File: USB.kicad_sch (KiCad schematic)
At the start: 38 parts, among them J1 DX07S024JJ2R1300, Q6 AGM612AP, Q7 AO3404A, U3 TPD4S480RUKR

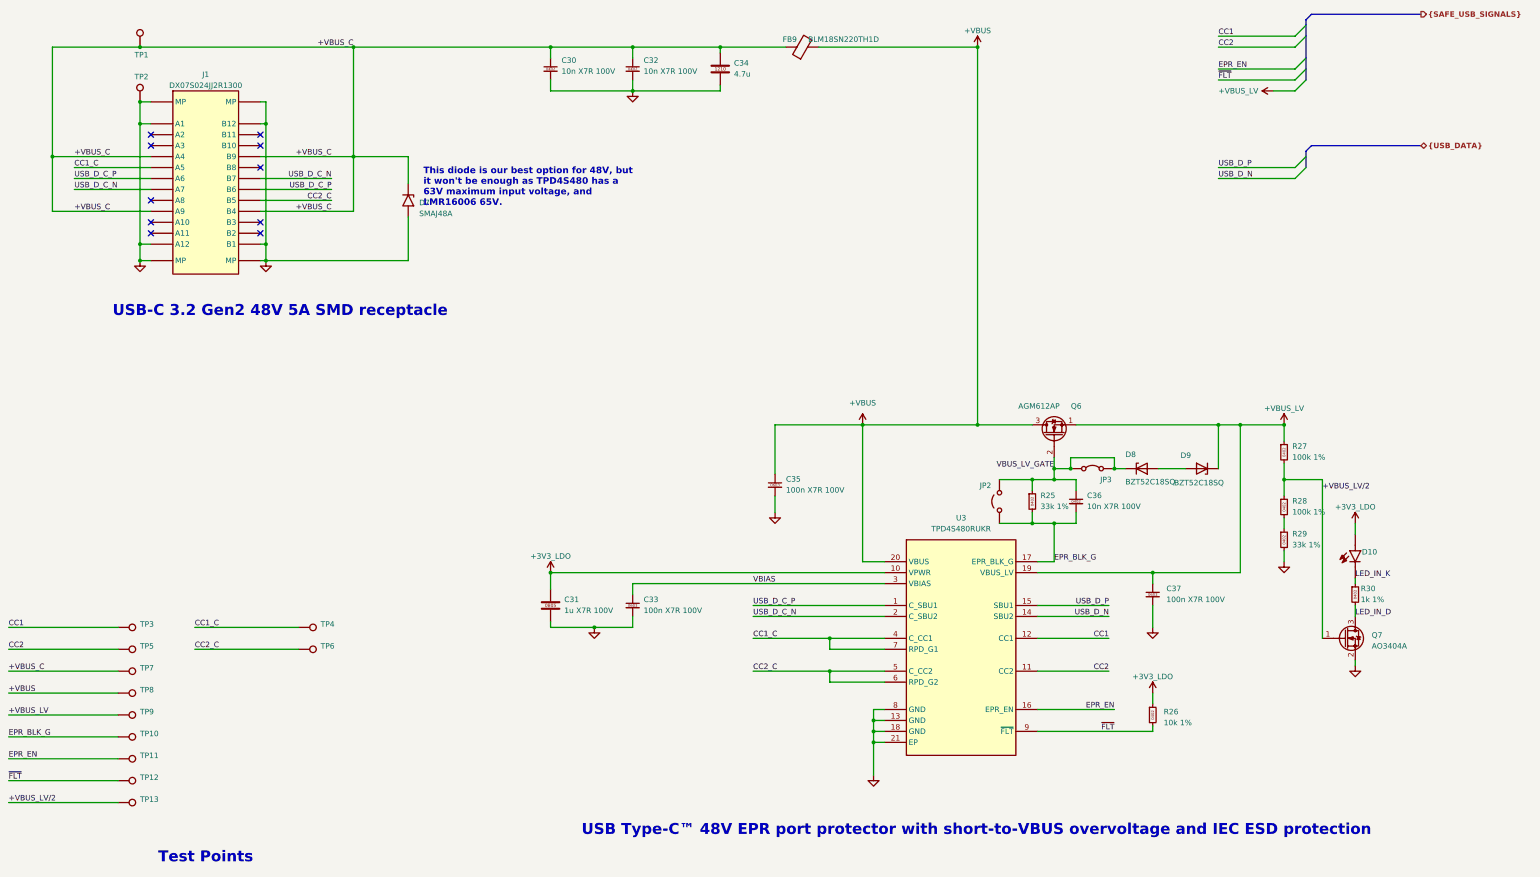
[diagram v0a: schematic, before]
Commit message: Cleaned up the hierarchy
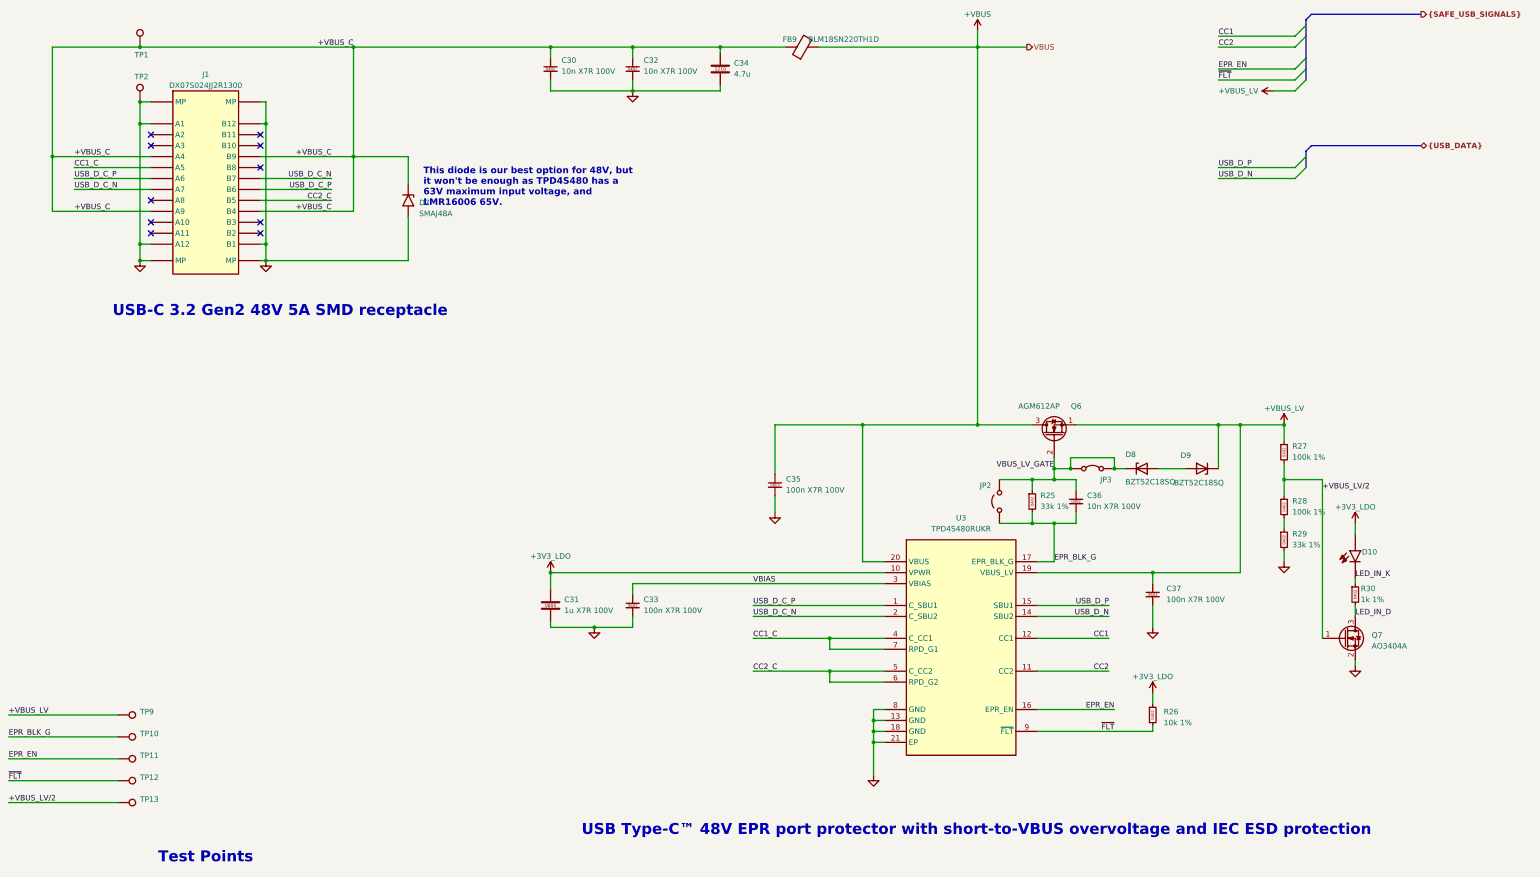
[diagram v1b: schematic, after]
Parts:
- removed TP3, TP4, TP5, TP6, TP7, TP8: tp_round_70, TestPoint:TestPoint_Pad_1.5x1.5mm, symbol Connector:TestPoint
- TP10, TP11, TP12, TP13, TP9: footprint TestPoint:TestPoint_Pad_1.5x1.5mm -> TestPoint:TestPoint_Pad_D1.0mm

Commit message: Starting with layout, oled, encoder, xt90
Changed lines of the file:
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@@
 	)
 	(bus_entry
-		(at 334.01 57.15)
+		(at 334.01 54.61)
 		(size 2.54 -2.54)
 		(stroke
@@
 	)
 	(bus_entry
-		(at 334.01 77.47)
+		(at 334.01 57.15)
 		(size 2.54 -2.54)
 		(stroke
@@
 	)
 	(bus_entry
-		(at 334.01 74.93)
+		(at 334.01 77.47)
 		(size 2.54 -2.54)
 		(stroke
@@
 	)
 	(bus_entry
-		(at 334.01 52.07)
+		(at 334.01 74.93)
 		(size 2.54 -2.54)
 		(stroke
@@
 	)
 	(bus_entry
-		(at 334.01 54.61)
+		(at 334.01 52.07)
 		(size 2.54 -2.54)
 		(stroke
@@
 	(wire
 		(pts
-			(xy 316.23 54.61) (xy 334.01 54.61)
-		)
-		(stroke
-			(width 0)
-			(type default)
-		)
-	)
-	(wire
-		(pts
 			(xy 95.25 64.77) (xy 93.98 64.77)
 		)
@@
 		)
 	)
-	(bus
-		(pts
-			(xy 336.55 54.61) (xy 336.55 52.07)
-		)
-		(stroke
-			(width 0)
-			(type default)
-		)
-	)
 	(wire
 		(pts
@@
 	(bus
 		(pts
-			(xy 336.55 52.07) (xy 336.55 49.53)
+			(xy 336.55 49.53) (xy 336.55 54.61)
 		)
 		(stroke
@@
 		)
 	)
+	(wire
+		(pts
+			(xy 316.23 54.61) (xy 334.01 54.61)
+		)
+		(stroke
+			(width 0)
+			(type default)
+		)
+	)
 	(image
 		(at 31.61 24.1795)
@@
 		)
 		(property "Value" "BLM18SN220TH1D"
-			(at 237.49 44.45 90)
+			(at 230.886 52.07 90)
 			(show_name no)
 			(do_not_autoplace no)

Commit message: Finished layout
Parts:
- removed Q7: AO3404A, Altium_port:sot-23-3L_103p_300x130x110_n, symbol Transistor_FET_Other:Q_NMOS_Depletion_GSD
- removed R30: 1k 1%, Resistor_SMD:R_0402_1005Metric, symbol 0_passives:R_0402
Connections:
- net LED_IN_K is gone; now on net GND: D10.1 (C)
- net +3V3_LDO: no longer D10.2 (A)
- net +VBUS_LV/2: no longer R27.2, R28.1
- net GND: no longer R29.2
- new net: D10.2 (A), R29.2
- new net: R27.2, R28.1
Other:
- note added: "(e.g. SMAJ58A or P6SMB60A)"
- moved on the sheet: D10, R28, R29

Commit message: Started routing
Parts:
- added D19: LED, LED_SMD:LED_0603_1608Metric, symbol Device:LED
- added R74: 10k, Resistor_SMD:R_0402_1005Metric, symbol Device:R
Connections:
- net +VBUS: now also D19.2 (A)
- net GND: now also R74.1
- new net: D19.1 (K), R74.2
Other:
- note removed: "Test Points"
- title: (none) -> Nitride-Nano

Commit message: Finished routing
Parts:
- removed TP10, TP13: tp_round_70, TestPoint:TestPoint_Pad_D1.0mm, symbol Connector:TestPoint
- JP3: footprint Altium_port:SolderJumper-2_P1.3mm_Bridged2Bar_RoundedPad1.0x1.5mm -> Jumper:SolderJumper-2_P1.3mm_Bridged2Bar_RoundedPad1.0x1.5mm
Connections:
- net VBUS_LV_GATE: no longer D8.1 (K), JP3.2 (B)
- new net: D8.1 (K), JP3.2 (B)
